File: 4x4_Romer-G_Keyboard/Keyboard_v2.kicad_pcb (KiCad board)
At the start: 2 copper layers, 100 x 100 mm, 43 parts

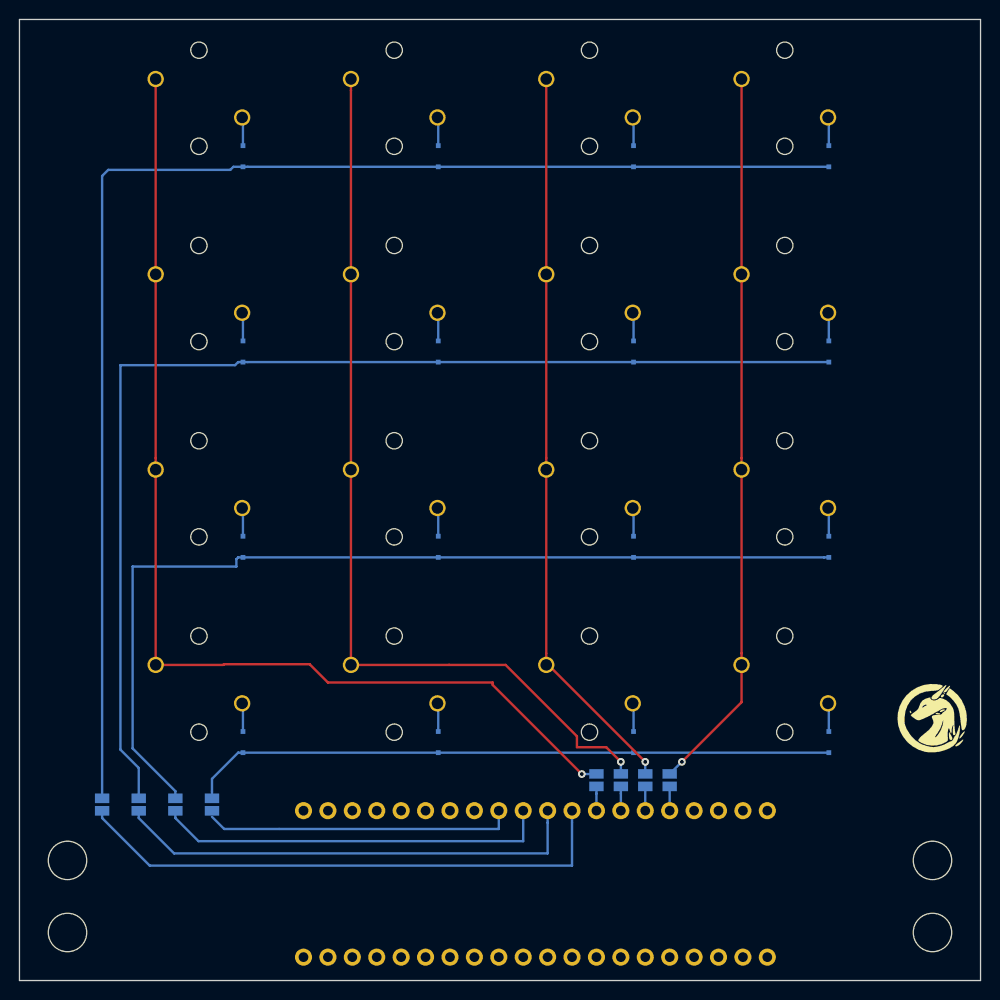
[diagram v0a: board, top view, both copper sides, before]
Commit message: Update Row and Col breaker
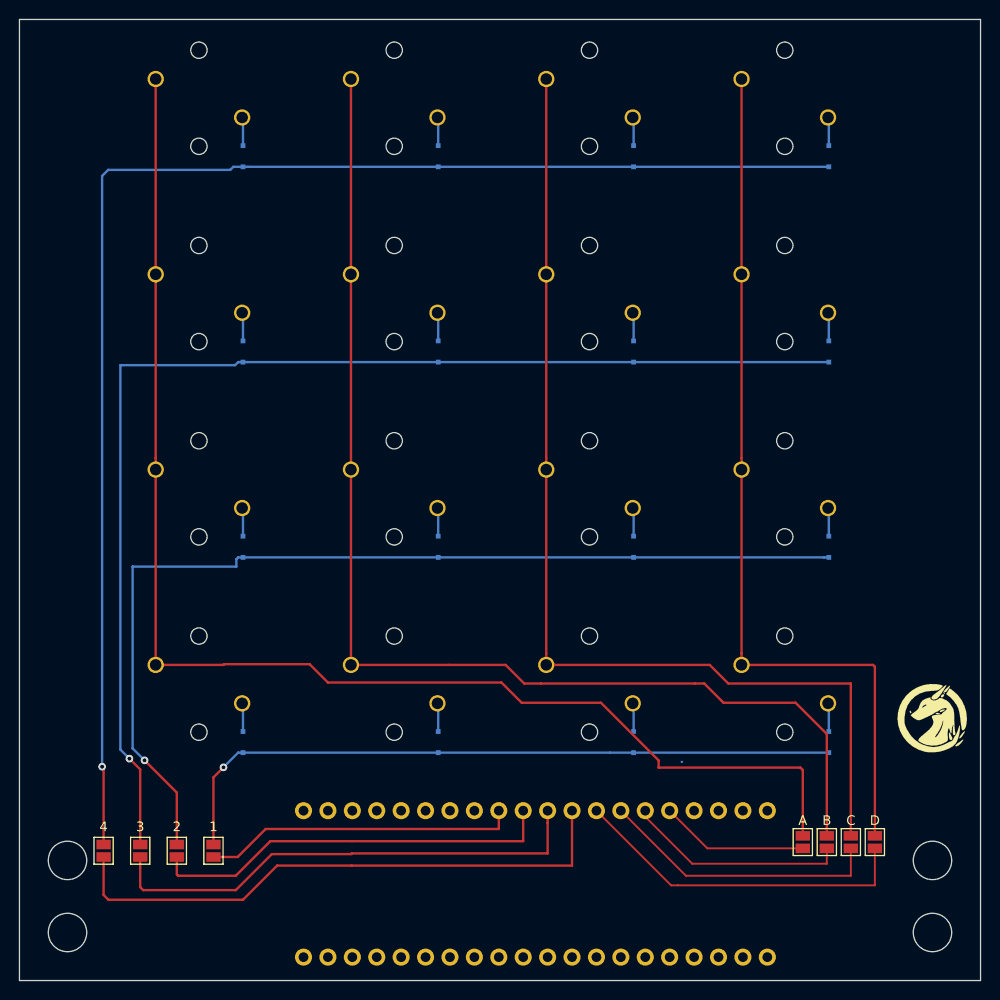
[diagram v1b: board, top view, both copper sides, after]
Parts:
- 1, 2, 3, 4, A, B, C, D: moved to F.Cu
- moved A 22.4 mm to (166.2, 129.0)
- moved B 22.4 mm to (168.8, 129.0)
- moved C 22.3 mm to (171.2, 129.0)
- moved D 22.3 mm to (173.8, 129.0)
- moved 1 4.81 mm to (104.9, 129.9)
- moved 2 4.81 mm to (101.1, 129.9)
- moved 3 4.81 mm to (97.3, 129.9)
- moved 4 4.81 mm to (93.5, 129.9)
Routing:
- net (no net): track 1013.5 -> 1241.4 mm
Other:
- net class Default removed
- board text added: "PA0 A PA1 B PA2 C PA3 D"
- board text removed: "PA0 D PA1 C PA2 B PA3 A"

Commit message: Fix Spacing
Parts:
- moved 4 2.00 mm to (95.5, 130.0)
- moved 3 1.19 mm to (98.5, 129.9)
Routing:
- net (no net): track 1241.4 -> 1239.5 mm
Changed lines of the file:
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@@
   )
   (footprint "Jumper:SolderJumper-2_P1.3mm_Open_Pad1.0x1.5mm" (layer "F.Cu")
-    (at 93.5 129.9 90)
+    (at 95.5 130 90)
     (descr "SMD Solder Jumper, 1x1.5mm Pads, 0.3mm gap, open")
     (tags "solder jumper open")
@@
   )
   (footprint "Jumper:SolderJumper-2_P1.3mm_Open_Pad1.0x1.5mm" (layer "F.Cu")
-    (at 97.31 129.9 90)
+    (at 98.5 129.9 90)
     (descr "SMD Solder Jumper, 1x1.5mm Pads, 0.3mm gap, open")
     (tags "solder jumper open")
@@
   (segment (start 168.75 131.25) (end 154.75 131.25) (width 0.2) (layer "F.Cu") (net 0))
   (segment (start 134.895 112.395) (end 137 114.5) (width 0.25) (layer "F.Cu") (net 0))
+  (segment (start 93.345 121.155) (end 95.5 123.31) (width 0.25) (layer "F.Cu") (net 0))
   (segment (start 139.558 109.359919) (end 139.558 90.242) (width 0.25) (layer "F.Cu") (net 0))
-  (segment (start 93.5 121.31) (end 93.5 129.25) (width 0.25) (layer "F.Cu") (net 0))
   (segment (start 135.327 110.562) (end 137.265 112.5) (width 0.25) (layer "F.Cu") (net 0))
+  (segment (start 95.75 135) (end 108 135) (width 0.25) (layer "F.Cu") (net 0))
   (segment (start 110.845 128.905) (end 107.25 132.5) (width 0.25) (layer "F.Cu") (net 0))
   (segment (start 152.55 133.5) (end 153.25 133.5) (width 0.2) (layer "F.Cu") (net 0))
   (segment (start 158 114.5) (end 165.5 114.5) (width 0.25) (layer "F.Cu") (net 0))
-  (segment (start 93.345 121.155) (end 93.5 121.31) (width 0.25) (layer "F.Cu") (net 0))
   (segment (start 139.7 126.987235) (end 139.7 125.73) (width 0.25) (layer "F.Cu") (net 0))
   (segment (start 116.84 112.395) (end 134.895 112.395) (width 0.25) (layer "F.Cu") (net 0))
@@
   (segment (start 168.75 129.65) (end 168.75 131.25) (width 0.2) (layer "F.Cu") (net 0))
   (segment (start 98.918 89.039919) (end 98.918 69.922) (width 0.25) (layer "F.Cu") (net 0))
+  (segment (start 95.5 134.75) (end 95.75 135) (width 0.25) (layer "F.Cu") (net 0))
   (segment (start 119.238 90.242) (end 119.238 110.562) (width 0.25) (layer "F.Cu") (net 0))
   (segment (start 147.32 125.73) (end 154.09 132.5) (width 0.2) (layer "F.Cu") (net 0))
@@
   (segment (start 110.365 127.635) (end 107.45 130.55) (width 0.25) (layer "F.Cu") (net 0))
   (segment (start 149.86 126.36) (end 149.86 125.73) (width 0.2) (layer "F.Cu") (net 0))
-  (segment (start 93.5 130.55) (end 93.5 134.5) (width 0.25) (layer "F.Cu") (net 0))
   (segment (start 159.878 90.242) (end 159.878 89.039919) (width 0.25) (layer "F.Cu") (net 0))
   (segment (start 114.935 110.49) (end 116.84 112.395) (width 0.25) (layer "F.Cu") (net 0))
   (segment (start 145.25 114.5) (end 151.25 120.5) (width 0.25) (layer "F.Cu") (net 0))
+  (segment (start 96.185 120.315) (end 98.5 122.63) (width 0.25) (layer "F.Cu") (net 0))
   (segment (start 134.62 127.635) (end 119.365 127.635) (width 0.25) (layer "F.Cu") (net 0))
   (segment (start 173.75 110.75) (end 173.75 128.35) (width 0.25) (layer "F.Cu") (net 0))
   (segment (start 98.918 90.242) (end 98.918 89.039919) (width 0.25) (layer "F.Cu") (net 0))
+  (segment (start 95.5 130.65) (end 95.5 134.75) (width 0.25) (layer "F.Cu") (net 0))
   (segment (start 165.5 114.5) (end 168.75 117.75) (width 0.25) (layer "F.Cu") (net 0))
   (segment (start 106.045 110.49) (end 114.935 110.49) (width 0.25) (layer "F.Cu") (net 0))
@@
   (segment (start 101.25 132.5) (end 101.12 132.37) (width 0.25) (layer "F.Cu") (net 0))
   (segment (start 142.24 126.987235) (end 142.24 125.73) (width 0.25) (layer "F.Cu") (net 0))
+  (segment (start 98.5 130.55) (end 98.5 133.5) (width 0.25) (layer "F.Cu") (net 0))
   (segment (start 107.25 134) (end 111 130.25) (width 0.25) (layer "F.Cu") (net 0))
+  (segment (start 98.5 133.5) (end 99 134) (width 0.25) (layer "F.Cu") (net 0))
   (segment (start 168.75 117.75) (end 168.75 128.35) (width 0.25) (layer "F.Cu") (net 0))
   (segment (start 119.238 50.804081) (end 119.238 69.922) (width 0.25) (layer "F.Cu") (net 0))
@@
   (segment (start 166.25 129.65) (end 156.32 129.65) (width 0.2) (layer "F.Cu") (net 0))
   (segment (start 137.265 112.5) (end 139 112.5) (width 0.25) (layer "F.Cu") (net 0))
+  (segment (start 99 134) (end 107.25 134) (width 0.25) (layer "F.Cu") (net 0))
   (segment (start 159.878 110.562) (end 159.878 109.359919) (width 0.25) (layer "F.Cu") (net 0))
   (segment (start 119.345 128.905) (end 110.845 128.905) (width 0.25) (layer "F.Cu") (net 0))
   (segment (start 119.238 69.922) (end 119.238 90.242) (width 0.25) (layer "F.Cu") (net 0))
   (segment (start 139.772 110.562) (end 139.558 110.562) (width 0.25) (layer "F.Cu") (net 0))
-  (segment (start 97.62 134) (end 107.25 134) (width 0.25) (layer "F.Cu") (net 0))
   (segment (start 158.5 112.5) (end 171.25 112.5) (width 0.25) (layer "F.Cu") (net 0))
   (segment (start 119.345 128.905) (end 137.16 128.905) (width 0.25) (layer "F.Cu") (net 0))
@@
   (segment (start 139.558 110.562) (end 156.562 110.562) (width 0.25) (layer "F.Cu") (net 0))
   (segment (start 139.558 89.039919) (end 139.558 69.922) (width 0.25) (layer "F.Cu") (net 0))
-  (segment (start 94 135) (end 108 135) (width 0.25) (layer "F.Cu") (net 0))
-  (segment (start 97.31 121.44) (end 97.31 129.25) (width 0.25) (layer "F.Cu") (net 0))
-  (segment (start 96.185 120.315) (end 97.31 121.44) (width 0.25) (layer "F.Cu") (net 0))
   (segment (start 101.12 132.37) (end 101.12 130.55) (width 0.25) (layer "F.Cu") (net 0))
-  (segment (start 97.31 130.55) (end 97.31 133.69) (width 0.25) (layer "F.Cu") (net 0))
   (segment (start 159.878 69.922) (end 159.878 49.602) (width 0.25) (layer "F.Cu") (net 0))
   (segment (start 142.24 131.445) (end 142.24 126.987235) (width 0.25) (layer "F.Cu") (net 0))
   (segment (start 155 112.5) (end 156 112.5) (width 0.25) (layer "F.Cu") (net 0))
-  (segment (start 97.31 133.69) (end 97.62 134) (width 0.25) (layer "F.Cu") (net 0))
   (segment (start 101.12 123.85) (end 101.12 129.25) (width 0.25) (layer "F.Cu") (net 0))
   (segment (start 98.918 110.562) (end 98.918 90.242) (width 0.25) (layer "F.Cu") (net 0))
   (segment (start 154.09 132.5) (end 171.25 132.5) (width 0.2) (layer "F.Cu") (net 0))
-  (segment (start 93.5 134.5) (end 94 135) (width 0.25) (layer "F.Cu") (net 0))
   (segment (start 129.468 110.562) (end 119.238 110.562) (width 0.25) (layer "F.Cu") (net 0))
+  (segment (start 95.5 123.31) (end 95.5 129.35) (width 0.25) (layer "F.Cu") (net 0))
   (segment (start 154.75 131.25) (end 149.86 126.36) (width 0.2) (layer "F.Cu") (net 0))
   (segment (start 105.973 110.562) (end 106.045 110.49) (width 0.25) (layer "F.Cu") (net 0))
@@
   (segment (start 173.75 133.5) (end 153.25 133.5) (width 0.2) (layer "F.Cu") (net 0))
   (segment (start 144.78 125.73) (end 152.55 133.5) (width 0.2) (layer "F.Cu") (net 0))
+  (segment (start 98.5 122.63) (end 98.5 129.25) (width 0.25) (layer "F.Cu") (net 0))
   (via (at 93.345 121.155) (size 0.8) (drill 0.4) (layers "F.Cu" "B.Cu") (net 0))
   (via (at 105.9725 121.2225) (size 0.8) (drill 0.4) (layers "F.Cu" "B.Cu") (net 0))

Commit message: update 4x4 keyboard
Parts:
- removed the   at (164.4, 112.6)
- removed 1, 2, 3, 4, A, B, C, D: SolderJumper-2_P1.3mm_Open_Pad1.0x1.5mm, Jumper:SolderJumper-2_P1.3mm_Open_Pad1.0x1.5mm
- removed D16: D_SOD-323F, Diode_SMD:D_SOD-323F
- removed REF**: ChinaBluePill, Arduino_BluePill_similar:ChinaBluePill
- added 7 SED LED: D1X8K, Display_7Segment:D1X8K, F.Cu at (160.0, 121.3)
- added 7 SEG LED: PinHeader_1x09_P2.54mm_Horizontal, Connector_PinHeader_2.54mm:PinHeader_1x09_P2.54mm_Horizontal, B.Cu at (138.2, 127.0)
- added COL: PinHeader_1x04_P2.54mm_Horizontal, Connector_PinHeader_2.54mm:PinHeader_1x04_P2.54mm_Horizontal, B.Cu at (123.8, 127.1)
- added ROW: PinHeader_1x04_P2.54mm_Horizontal, Connector_PinHeader_2.54mm:PinHeader_1x04_P2.54mm_Horizontal, B.Cu at (111.1, 127.1)
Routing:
- net (no net): track 1239.5 -> 1133.8 mm, vias 4 -> 0
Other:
- outline, holes or cut-outs redrawn
- board text added: "1 2 3 4"
- board text added: "7 SEG LED 0,56{dblquote} 14,22mm"
- board text added: "D C B A"
- board text added: "D1-D15 1N 4148 WS SOD-323F"
- board text added: "DP A B C D E F G GND"
- board text removed: "D1-D16 1N 4148 WS SOD-323F"
- board text removed: "PA0 A PA1 B PA2 C PA3 D"
- board text removed: "PA4 4 PA5 3 PA6 2 PA7 1"
